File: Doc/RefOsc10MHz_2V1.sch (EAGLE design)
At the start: 73 parts, among them CON1 TYCO-AMP_USBUSB-B_SMT, CON11 MCX-J-P-X-RA-SM1, CON2 HEADER-2X5SMD, CON3 SD-73100-0105, CON4 AVR-ISP-6SMD, CON5 AVR-JTAG-10SMD, CON6 HEADER-2X3SMD, IC1 ATmega328-P, IC11 712-RXM-GNSS-TM-B, IC2 LC4032V_XXT44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

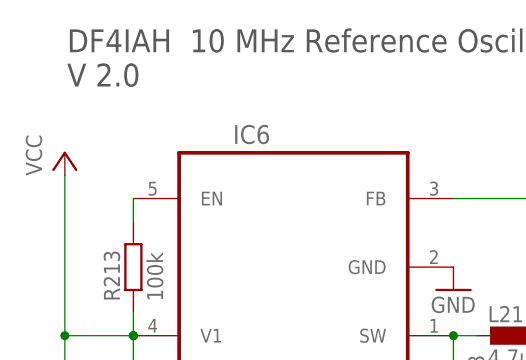
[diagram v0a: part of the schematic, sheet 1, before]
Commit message: avr_DF4IAH_Bootloader - Doc - Eagle: V2.1 after manufacturing by PCB-Pool - findings to be fixed
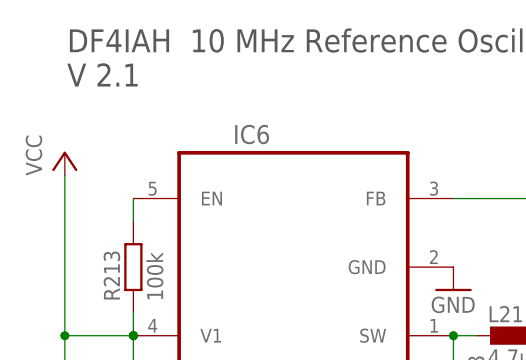
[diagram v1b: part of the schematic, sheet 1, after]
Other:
- note added: "DF4IAH 10 MHz Reference Oscillator V 2.1"
- note removed: "DF4IAH 10 MHz Reference Oscillator V 2.0"
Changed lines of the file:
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@@
 <text x="203.962" y="110.236" size="1.27" layer="97">2.5 MHz out</text>
 <text x="10.414" y="258.826" size="2.54" layer="97">DF4IAH  10 MHz Reference Oscillator
-V 2.0</text>
+V 2.1</text>
 <text x="64.516" y="110.998" size="1.778" layer="97">USB Disconnect</text>
 <text x="107.696" y="89.916" size="1.778" layer="97">USB D-</text>
@@
 <wire x1="127" y1="218.44" x2="127" y2="215.9" width="0.1524" layer="91"/>
 <pinref part="CON3" gate="G$1" pin="3"/>
+<pinref part="CON3" gate="G$1" pin="3"/>
+<junction x="127" y="218.44"/>
 <pinref part="CON3" gate="G$1" pin="2"/>
-<junction x="127" y="218.44"/>
-</segment>
-<segment>
+</segment>
+<segment>

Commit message: avr_DF4IAH_Bootloader - Doc - Eagle: V2.1 after manufacturing by PCB-Pool - findings to be fixed (2) - BNC-Drills size doubled, Goldcap bigger than assumed, switching converter had wrong PIN assignment, now with grounded bottom layer
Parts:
- added H1, H2, H3, H4: MOUNT-PAD-ROUND2.8, holes:MOUNT-PAD-ROUND2.8
- C81: device rcl:CPOL-EUC -> rcl:CPOL-EU140CLH-1010
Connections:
- net GND: now also H1.MOUNT, H2.MOUNT, H3.MOUNT, H4.MOUNT
- net VCC: now also IC6.VIN; no longer IC6.V1
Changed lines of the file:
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@@
 <part name="GND16" library="supply1" deviceset="GND" device=""/>
 <part name="C1" library="rcl" deviceset="CPOL-EU" device="C" value="47uF"/>
-<part name="C81" library="rcl" deviceset="CPOL-EU" device="C" value="0.22F"/>
 <part name="D1" library="diode" deviceset="BZX84CSMD" device="" value="BZX84-C3V6"/>
 <part name="D2" library="diode" deviceset="BZX84CSMD" device="" value="BZX84-C3V6"/>
@@
 <part name="CON1" library="df4iah" deviceset="TYCO-AMP_USB" device="USB-B_SMT"/>
 <part name="CON4" library="atmel-1" deviceset="AVR-ISP-6" device="SMD"/>
+<part name="H1" library="holes" deviceset="MOUNT-PAD-ROUND" device="2.8"/>
+<part name="H2" library="holes" deviceset="MOUNT-PAD-ROUND" device="2.8"/>
+<part name="H3" library="holes" deviceset="MOUNT-PAD-ROUND" device="2.8"/>
+<part name="H4" library="holes" deviceset="MOUNT-PAD-ROUND" device="2.8"/>
+<part name="GND13" library="supply1" deviceset="GND" device=""/>
+<part name="GND19" library="supply1" deviceset="GND" device=""/>
+<part name="GND23" library="supply1" deviceset="GND" device=""/>
+<part name="GND24" library="supply1" deviceset="GND" device=""/>
+<part name="C81" library="rcl" deviceset="CPOL-EU" device="140CLH-1010" value="0.22F"/>
 </parts>
 <sheets>
@@
  6 GND</text>
 <text x="133.604" y="239.268" size="1.778" layer="94">I2C</text>
+<rectangle x1="289.56" y1="-15.24" x2="424.18" y2="50.8" layer="98"/>
 </plain>
 <instances>
@@
 <instance part="GND16" gate="1" x="241.3" y="177.8"/>
 <instance part="C1" gate="G$1" x="38.1" y="101.6"/>
-<instance part="C81" gate="G$1" x="241.3" y="190.5" smashed="yes">
-<attribute name="NAME" x="234.823" y="188.4426" size="1.778" layer="95"/>
-<attribute name="VALUE" x="234.823" y="185.9026" size="1.778" layer="96"/>
-</instance>
 <instance part="D1" gate="G$1" x="33.02" y="76.2" rot="R90"/>
 <instance part="D2" gate="G$1" x="50.8" y="76.2" rot="R90"/>
@@
 </instance>
 <instance part="CON4" gate="G$1" x="187.96" y="124.46"/>
+<instance part="H1" gate="G$1" x="320.04" y="38.1"/>
+<instance part="H2" gate="G$1" x="320.04" y="2.54"/>
+<instance part="H3" gate="G$1" x="388.62" y="2.54"/>
+<instance part="H4" gate="G$1" x="388.62" y="38.1"/>
+<instance part="GND13" gate="1" x="312.42" y="0"/>
+<instance part="GND19" gate="1" x="312.42" y="35.56"/>
+<instance part="GND23" gate="1" x="381" y="35.56"/>
+<instance part="GND24" gate="1" x="381" y="0"/>
+<instance part="C81" gate="G$1" x="241.3" y="190.5"/>
 </instances>
 <busses>
@@
 <junction x="119.38" y="238.76"/>
 </segment>
+<segment>
+<pinref part="GND19" gate="1" pin="GND"/>
+<pinref part="H1" gate="G$1" pin="MOUNT"/>
+<wire x1="312.42" y1="38.1" x2="317.5" y2="38.1" width="0.1524" layer="91"/>
+</segment>
+<segment>
+<pinref part="GND13" gate="1" pin="GND"/>
+<pinref part="H2" gate="G$1" pin="MOUNT"/>
+<wire x1="312.42" y1="2.54" x2="317.5" y2="2.54" width="0.1524" layer="91"/>
+</segment>
+<segment>
+<pinref part="GND23" gate="1" pin="GND"/>
+<pinref part="H4" gate="G$1" pin="MOUNT"/>
+<wire x1="381" y1="38.1" x2="386.08" y2="38.1" width="0.1524" layer="91"/>
+</segment>
+<segment>
+<pinref part="GND24" gate="1" pin="GND"/>
+<pinref part="H3" gate="G$1" pin="MOUNT"/>
+<wire x1="381" y1="2.54" x2="386.08" y2="2.54" width="0.1524" layer="91"/>
+</segment>
 </net>
 <net name="VCC" class="2">
@@
 <junction x="10.16" y="198.12"/>
 <pinref part="L31" gate="G$1" pin="2"/>
-<pinref part="IC6" gate="A" pin="V1"/>
+<pinref part="IC6" gate="A" pin="VIN"/>
 </segment>
 <segment>
@@
 <wire x1="215.9" y1="220.98" x2="241.3" y2="220.98" width="0.1524" layer="91"/>
 <wire x1="241.3" y1="220.98" x2="241.3" y2="200.66" width="0.1524" layer="91"/>
-<pinref part="C81" gate="G$1" pin="+"/>
 <wire x1="241.3" y1="200.66" x2="241.3" y2="193.04" width="0.1524" layer="91"/>
 <wire x1="241.3" y1="200.66" x2="236.22" y2="200.66" width="0.1524" layer="91"/>
@@
 <junction x="241.3" y="220.98"/>
 <pinref part="D82" gate="G$1" pin="C"/>
-</segment>
-</net>
+<pinref part="C81" gate="G$1" pin="+"/>
+</segment>
+</net>

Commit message: avr_DF4IAH_Bootloader - Doc - Eagle: V2.1 after manufacturing by PCB-Pool - findings to be fixed (3) - take big C211 from bottom to top.
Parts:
- D211, D82: value CRS08 -> CRS80; device diode:ZENER-DIODESOT23 -> diode:ZENER-DIODESOD80C
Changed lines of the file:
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@@
 <part name="R212" library="rcl" deviceset="R-EU_" device="R0805" value="10k"/>
 <part name="R213" library="rcl" deviceset="R-EU_" device="R0805" value="100k"/>
-<part name="D211" library="diode" deviceset="ZENER-DIODE" device="SOT23" value="CRS08"/>
 <part name="C212" library="rcl" deviceset="CPOL-EU" device="A/3216-18W" value="22uF"/>
 <part name="C213" library="rcl" deviceset="CPOL-EU" device="A/3216-18W" value="22uF"/>
@@
 <part name="L31" library="rcl" deviceset="L-EU" device="L1812" value="10uH"/>
 <part name="IC6" library="df4iah" deviceset="LM2831" device="" technology="YMF" value="LM2831YMF"/>
-<part name="D82" library="diode" deviceset="ZENER-DIODE" device="SOT23" value="CRS08"/>
 <part name="R25" library="rcl" deviceset="R-EU_" device="R0805" value="2.7k"/>
 <part name="R221" library="rcl" deviceset="R-EU_" device="R0805" value="56"/>
@@
 <part name="GND24" library="supply1" deviceset="GND" device=""/>
 <part name="C81" library="rcl" deviceset="CPOL-EU" device="140CLH-1010" value="0.22F"/>
+<part name="D211" library="diode" deviceset="ZENER-DIODE" device="SOD80C" value="CRS80"/>
+<part name="D82" library="diode" deviceset="ZENER-DIODE" device="SOD80C" value="CRS80"/>
 </parts>
 <sheets>
@@
 <instance part="R212" gate="G$1" x="63.5" y="213.36"/>
 <instance part="R213" gate="G$1" x="17.78" y="238.76" rot="R90"/>
-<instance part="D211" gate="G$1" x="53.34" y="223.52" rot="R90"/>
 <instance part="C212" gate="G$1" x="35.56" y="213.36"/>
 <instance part="C213" gate="G$1" x="45.72" y="213.36"/>
@@
 <instance part="L31" gate="G$1" x="38.1" y="175.26" rot="R270"/>
 <instance part="IC6" gate="A" x="35.56" y="238.76"/>
-<instance part="D82" gate="G$1" x="236.22" y="203.2" rot="R270"/>
 <instance part="R25" gate="G$1" x="111.76" y="22.86"/>
 <instance part="R221" gate="G$1" x="86.36" y="241.3" smashed="yes" rot="R270">
@@
 <instance part="GND24" gate="1" x="381" y="0"/>
 <instance part="C81" gate="G$1" x="241.3" y="190.5"/>
+<instance part="D211" gate="G$1" x="53.34" y="223.52" rot="R90"/>
+<instance part="D82" gate="G$1" x="236.22" y="203.2" rot="R270"/>
 </instances>
 <busses>
@@
 <wire x1="45.72" y1="205.74" x2="53.34" y2="205.74" width="0.1524" layer="91"/>
 <junction x="45.72" y="205.74"/>
-<pinref part="D211" gate="G$1" pin="A"/>
 <wire x1="53.34" y1="205.74" x2="58.42" y2="205.74" width="0.1524" layer="91"/>
 <wire x1="58.42" y1="205.74" x2="73.66" y2="205.74" width="0.1524" layer="91"/>
@@
 <junction x="58.42" y="205.74"/>
 <pinref part="IC4" gate="&gt;NAME" pin="GND"/>
+<pinref part="D211" gate="G$1" pin="A"/>
 </segment>
 <segment>
@@
 <label x="251.46" y="233.68" size="1.778" layer="95" rot="R90" xref="yes"/>
 <junction x="241.3" y="220.98"/>
+<pinref part="C81" gate="G$1" pin="+"/>
 <pinref part="D82" gate="G$1" pin="C"/>
-<pinref part="C81" gate="G$1" pin="+"/>
 </segment>
 </net>
@@
 <net name="SW" class="1">
 <segment>
-<pinref part="D211" gate="G$1" pin="C"/>
 <wire x1="53.34" y1="226.06" x2="53.34" y2="231.14" width="0.1524" layer="91"/>
 <pinref part="L211" gate="G$1" pin="2"/>
@@
 <pinref part="IC6" gate="A" pin="SW"/>
 <junction x="53.34" y="231.14"/>
-</segment>
-</net>
+<pinref part="D211" gate="G$1" pin="C"/>
+</segment>
+</net>

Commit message: avr_DF4IAH_Bootloader - Doc - Eagle: V2.1 after manufacturing by PCB-Pool - findings to be fixed (4) - change R81 from 1k to 150Ohm, 3.3V regulator corrected.
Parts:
- R211: value 10k -> 45.3k
- R81: value 1k -> 150
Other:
- moved on the sheet: C221, D221, R221
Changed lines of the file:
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@@
 <part name="R3" library="rcl" deviceset="R-EU_" device="R0805" value="1.5k"/>
 <part name="R4" library="rcl" deviceset="R-EU_" device="R0805" value="1M"/>
-<part name="R81" library="rcl" deviceset="R-EU_" device="R0805" value="1k"/>
+<part name="R81" library="rcl" deviceset="R-EU_" device="R0805" value="150"/>
 <part name="R13" library="rcl" deviceset="R-EU_" device="R0805" value="15k"/>
 <part name="R41" library="rcl" deviceset="R-EU_" device="R0805" value="12k"/>
@@
 <part name="C951" library="rcl" deviceset="C-EU" device="C0805" value="10n"/>
 <part name="C22" library="rcl" deviceset="CPOL-EU" device="B" value="10uF"/>
-<part name="R211" library="rcl" deviceset="R-EU_" device="R0805" value="10k"/>
+<part name="R211" library="rcl" deviceset="R-EU_" device="R0805" value="45.3k"/>
 <part name="R212" library="rcl" deviceset="R-EU_" device="R0805" value="10k"/>
 <part name="R213" library="rcl" deviceset="R-EU_" device="R0805" value="100k"/>
@@
 <part name="IC6" library="df4iah" deviceset="LM2831" device="" technology="YMF" value="LM2831YMF"/>
 <part name="R25" library="rcl" deviceset="R-EU_" device="R0805" value="2.7k"/>
-<part name="R221" library="rcl" deviceset="R-EU_" device="R0805" value="56"/>
-<part name="D221" library="diode" deviceset="BZX84CSMD" device="" value="BZX84-C3V0"/>
 <part name="GND12" library="supply1" deviceset="GND" device=""/>
 <part name="C221" library="rcl" deviceset="C-EU" device="C0805" value="100n"/>
@@
 <part name="D211" library="diode" deviceset="ZENER-DIODE" device="SOD80C" value="CRS80"/>
 <part name="D82" library="diode" deviceset="ZENER-DIODE" device="SOD80C" value="CRS80"/>
+<part name="D221" library="diode" deviceset="BZX84CSMD" device="" value="BZX84-C3V0"/>
+<part name="R221" library="rcl" deviceset="R-EU_" device="R0805" value="56"/>
 </parts>
 <sheets>
@@
 <instance part="IC6" gate="A" x="35.56" y="238.76"/>
 <instance part="R25" gate="G$1" x="111.76" y="22.86"/>
-<instance part="R221" gate="G$1" x="86.36" y="241.3" smashed="yes" rot="R270">
-<attribute name="NAME" x="83.0326" y="244.602" size="1.778" layer="95" rot="R270"/>
-<attribute name="VALUE" x="87.884" y="241.3" size="1.778" layer="96" rot="R270"/>
-</instance>
-<instance part="D221" gate="G$1" x="104.14" y="246.38" smashed="yes" rot="R180">
-<attribute name="NAME" x="107.188" y="250.571" size="1.778" layer="95" rot="R180"/>
-<attribute name="VALUE" x="109.982" y="243.713" size="1.778" layer="96" rot="R180"/>
-</instance>
 <instance part="GND12" gate="1" x="111.76" y="236.22"/>
-<instance part="C221" gate="G$1" x="101.6" y="238.76" smashed="yes" rot="R90">
-<attribute name="NAME" x="106.68" y="236.22" size="1.778" layer="95" rot="R180"/>
-<attribute name="VALUE" x="106.68" y="233.68" size="1.778" layer="96" rot="R180"/>
+<instance part="C221" gate="G$1" x="96.52" y="238.76" smashed="yes" rot="R90">
+<attribute name="NAME" x="101.6" y="236.22" size="1.778" layer="95" rot="R180"/>
+<attribute name="VALUE" x="101.6" y="233.68" size="1.778" layer="96" rot="R180"/>
 </instance>
 <instance part="IC4" gate="&gt;NAME" x="96.52" y="215.9"/>
@@
 <instance part="D211" gate="G$1" x="53.34" y="223.52" rot="R90"/>
 <instance part="D82" gate="G$1" x="236.22" y="203.2" rot="R270"/>
+<instance part="D221" gate="G$1" x="99.06" y="246.38" smashed="yes" rot="R180">
+<attribute name="NAME" x="97.282" y="248.285" size="1.778" layer="95"/>
+<attribute name="VALUE" x="89.662" y="242.951" size="1.778" layer="96"/>
+</instance>
+<instance part="R221" gate="G$1" x="81.28" y="246.38"/>
 </instances>
 <busses>
@@
 <pinref part="GND12" gate="1" pin="GND"/>
 <wire x1="111.76" y1="238.76" x2="111.76" y2="246.38" width="0.1524" layer="91"/>
-<pinref part="D221" gate="G$1" pin="A"/>
-<wire x1="111.76" y1="246.38" x2="106.68" y2="246.38" width="0.1524" layer="91"/>
+<wire x1="111.76" y1="246.38" x2="101.6" y2="246.38" width="0.1524" layer="91"/>
 <pinref part="C221" gate="G$1" pin="2"/>
-<wire x1="111.76" y1="238.76" x2="106.68" y2="238.76" width="0.1524" layer="91"/>
+<wire x1="111.76" y1="238.76" x2="101.6" y2="238.76" width="0.1524" layer="91"/>
 <wire x1="111.76" y1="238.76" x2="119.38" y2="238.76" width="0.1524" layer="91"/>
 <wire x1="119.38" y1="238.76" x2="149.86" y2="238.76" width="0.1524" layer="91"/>
@@
 <wire x1="119.38" y1="248.92" x2="134.62" y2="248.92" width="0.1524" layer="91"/>
 <junction x="119.38" y="238.76"/>
+<pinref part="D221" gate="G$1" pin="A"/>
 </segment>
 <segment>
@@
 <wire x1="170.18" y1="231.14" x2="170.18" y2="233.68" width="0.1524" layer="91"/>
 <label x="170.18" y="233.68" size="1.778" layer="95" rot="R90" xref="yes"/>
-<pinref part="R221" gate="G$1" pin="1"/>
-<wire x1="86.36" y1="246.38" x2="73.66" y2="246.38" width="0.1524" layer="91"/>
+<wire x1="76.2" y1="246.38" x2="73.66" y2="246.38" width="0.1524" layer="91"/>
 <junction x="73.66" y="246.38"/>
 <pinref part="D202" gate="G$1" pin="C"/>
@@
 <wire x1="127" y1="243.84" x2="134.62" y2="243.84" width="0.1524" layer="91"/>
 <junction x="127" y="231.14"/>
+<pinref part="R221" gate="G$1" pin="1"/>
 </segment>
 </net>
@@
 <net name="+3V0" class="1">
 <segment>
+<wire x1="96.52" y1="246.38" x2="86.36" y2="246.38" width="0.1524" layer="91"/>
+<wire x1="86.36" y1="218.44" x2="86.36" y2="238.76" width="0.1524" layer="91"/>
+<wire x1="86.36" y1="238.76" x2="86.36" y2="246.38" width="0.1524" layer="91"/>
+<pinref part="C221" gate="G$1" pin="1"/>
+<wire x1="86.36" y1="238.76" x2="93.98" y2="238.76" width="0.1524" layer="91"/>
+<pinref part="IC4" gate="&gt;NAME" pin="VCC_3V0"/>
+<junction x="86.36" y="238.76"/>
 <pinref part="D221" gate="G$1" pin="C"/>
 <pinref part="R221" gate="G$1" pin="2"/>
-<wire x1="101.6" y1="246.38" x2="93.98" y2="246.38" width="0.1524" layer="91"/>
-<wire x1="86.36" y1="218.44" x2="86.36" y2="236.22" width="0.1524" layer="91"/>
-<wire x1="86.36" y1="236.22" x2="93.98" y2="236.22" width="0.1524" layer="91"/>
-<wire x1="93.98" y1="236.22" x2="93.98" y2="238.76" width="0.1524" layer="91"/>
-<wire x1="93.98" y1="238.76" x2="93.98" y2="246.38" width="0.1524" layer="91"/>
-<pinref part="C221" gate="G$1" pin="1"/>
-<wire x1="93.98" y1="238.76" x2="99.06" y2="238.76" width="0.1524" layer="91"/>
-<pinref part="IC4" gate="&gt;NAME" pin="VCC_3V0"/>
-<junction x="93.98" y="238.76"/>
-<junction x="86.36" y="236.22"/>
-</segment>
-</net>
+<junction x="86.36" y="246.38"/>
+</segment>
+</net>
